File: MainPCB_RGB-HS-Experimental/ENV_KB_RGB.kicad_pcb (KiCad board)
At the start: 2 copper layers, 347 x 156.1 mm, 198 parts

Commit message: fixed components that were no longer connected and added cutouts for directly soldering MCU onto PCB
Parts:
- removed the RPI0 at (267.1, 74.7)
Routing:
- net row6: track 365.1 -> 366.3 mm
- net row5: track 352.1 -> 353.2 mm
- net row4: track 327.2 -> 328.3 mm
- net row3: track 370.7 -> 371.7 mm
- net row2: track 374.1 -> 374.9 mm
- net row0: track 381.1 -> 382.0 mm
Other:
- outline, holes or cut-outs redrawn
- board text added: "DOM"
- board text added: "https://github.com/envious-data Revision 1.2 EnvKB TKL HS"

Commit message: minor markers and tweaks
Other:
- board text added: "PWR"
- board text added: "https://github.com/envious-data Revision 1.2 EnvKB TKL HS | Envious#0739"
- board text removed: "https://github.com/envious-data Revision 1.2 EnvKB TKL HS"
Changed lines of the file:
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@@
   (general
     (thickness 1.6)
-    (drawings 1943)
+    (drawings 1946)
     (tracks 2057)
     (zones 0)
@@
     )
   )
+  (gr_line (start 246.75 82.203) (end 246.75 85.2) (layer F.SilkS) (width 0.12))
+  (gr_line (start 244.217 82.203) (end 246.75 82.203) (layer F.SilkS) (width 0.12))
+  (gr_text PWR (at 191.5 67.3) (layer F.SilkS)
+    (effects (font (size 1 1) (thickness 0.15)))
+  )
   (gr_text DOM (at 153.55 69.15) (layer F.SilkS)
     (effects (font (size 0.8 0.8) (thickness 0.15)))
   )
-  (gr_text "https://github.com/envious-data\nRevision 1.2\nEnvKB TKL HS" (at 247.15 74.7) (layer F.Cu)
+  (gr_text "https://github.com/envious-data\nRevision 1.2\nEnvKB TKL HS | Envious#0739" (at 247.15 74.7) (layer F.Cu)
     (effects (font (size 1.5 1.5) (thickness 0.3)) (justify left))
   )

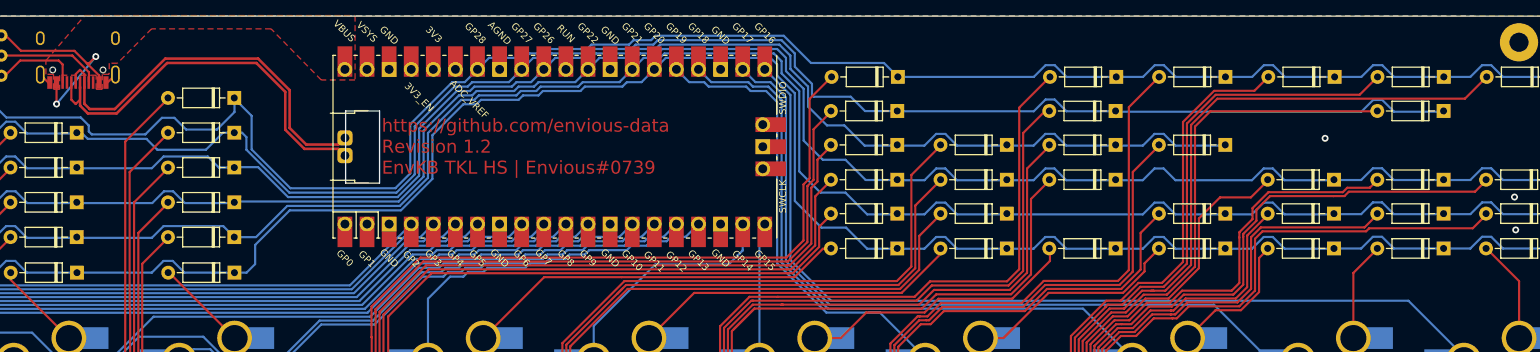
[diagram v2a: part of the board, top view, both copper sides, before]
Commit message: small tweaks to some traces and spacing
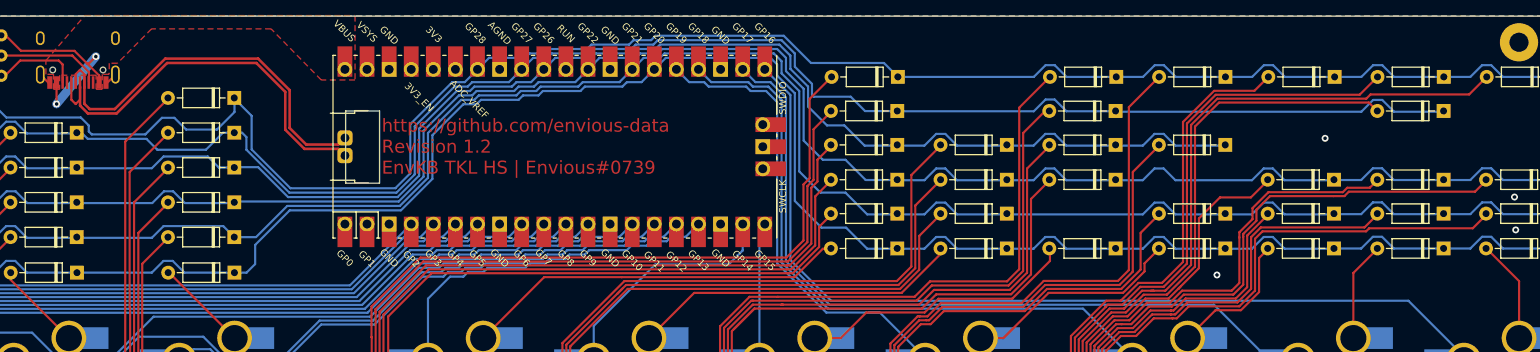
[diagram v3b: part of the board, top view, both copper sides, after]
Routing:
- net Net-(D77-Pad2): track 203.2 -> 204.0 mm
- net GND: vias 3 -> 4
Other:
- board text added: "GP0"
- board text added: "GP1"
